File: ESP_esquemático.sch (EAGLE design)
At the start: 10 parts, among them U1 GY-521MPU6050

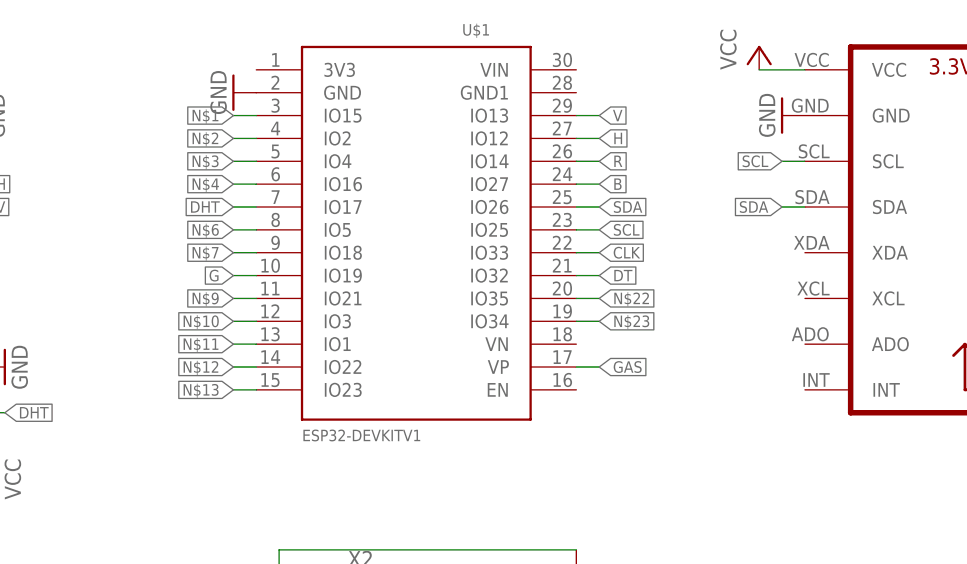
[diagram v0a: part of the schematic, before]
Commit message: adicionado código do arm
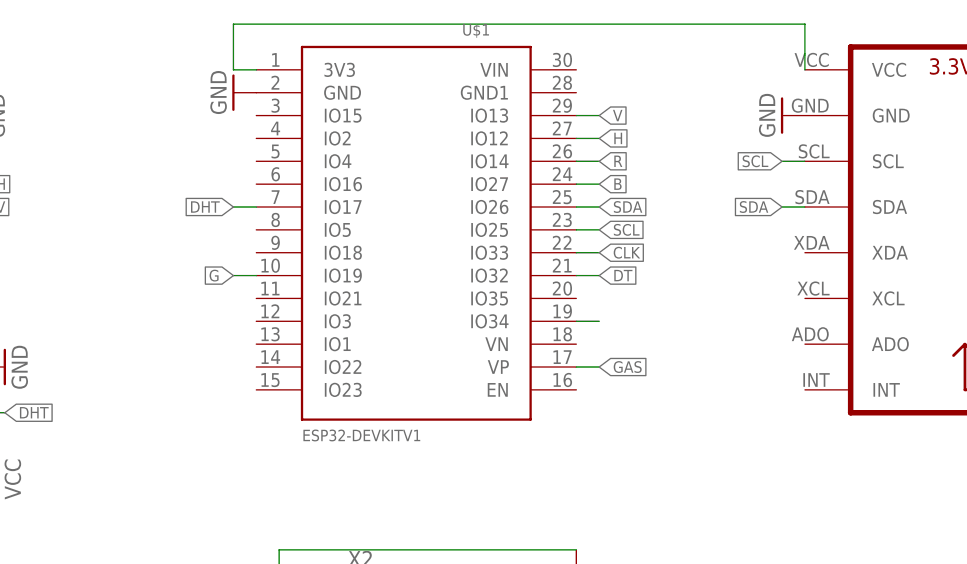
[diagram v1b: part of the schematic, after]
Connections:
- removed net N$10: U$1.IO3
- removed net N$11: U$1.IO1
- removed net N$12: U$1.IO22
- removed net N$13: U$1.IO23
- removed net N$2: U$1.IO2
- removed net N$22: U$1.IO35
- removed net N$3: U$1.IO4
- removed net N$4: U$1.IO16
- removed net N$6: U$1.IO5
- removed net N$7: U$1.IO18
- removed net N$9: U$1.IO21
- net N$1: now also U$1.3V3, U1.VCC; no longer U$1.IO15
- net VCC: no longer U1.VCC
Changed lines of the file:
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@@
 <part name="P+2" library="supply1" deviceset="VCC" device=""/>
 <part name="P+3" library="supply1" deviceset="VCC" device=""/>
-<part name="P+4" library="supply1" deviceset="VCC" device=""/>
 <part name="R1" library="rcl" deviceset="R-US_" device="0204/7" value="3k9"/>
 <part name="R2" library="rcl" deviceset="R-US_" device="0204/7" value="3k9"/>
@@
 <instance part="P+2" gate="VCC" x="33.02" y="10.16" rot="R90"/>
 <instance part="P+3" gate="VCC" x="2.54" y="30.48" rot="R180"/>
-<instance part="P+4" gate="VCC" x="88.9" y="78.74"/>
 <instance part="R1" gate="G$1" x="68.58" y="17.78" rot="R90"/>
 <instance part="R2" gate="G$1" x="71.12" y="0" rot="R90"/>
@@
 <wire x1="2.54" y1="33.02" x2="2.54" y2="35.56" width="0.1524" layer="91"/>
 </segment>
-<segment>
-<pinref part="U1" gate="G$1" pin="VCC"/>
-<pinref part="P+4" gate="VCC" pin="VCC"/>
-<wire x1="88.9" y1="76.2" x2="93.98" y2="76.2" width="0.1524" layer="91"/>
-</segment>
-</net>
-<net name="N$1" class="0">
-<segment>
-<pinref part="U$1" gate="G$1" pin="IO15"/>
-<wire x1="33.02" y1="71.12" x2="30.48" y2="71.12" width="0.1524" layer="91"/>
-<label x="30.48" y="71.12" size="1.27" layer="95" rot="R180" xref="yes"/>
-</segment>
-</net>
-<net name="N$2" class="0">
-<segment>
-<pinref part="U$1" gate="G$1" pin="IO2"/>
-<wire x1="33.02" y1="68.58" x2="30.48" y2="68.58" width="0.1524" layer="91"/>
-<label x="30.48" y="68.58" size="1.27" layer="95" rot="R180" xref="yes"/>
-</segment>
-</net>
-<net name="N$3" class="0">
-<segment>
-<pinref part="U$1" gate="G$1" pin="IO4"/>
-<wire x1="33.02" y1="66.04" x2="30.48" y2="66.04" width="0.1524" layer="91"/>
-<label x="30.48" y="66.04" size="1.27" layer="95" rot="R180" xref="yes"/>
-</segment>
-</net>
-<net name="N$4" class="0">
-<segment>
-<pinref part="U$1" gate="G$1" pin="IO16"/>
-<wire x1="33.02" y1="63.5" x2="30.48" y2="63.5" width="0.1524" layer="91"/>
-<label x="30.48" y="63.5" size="1.27" layer="95" rot="R180" xref="yes"/>
-</segment>
-</net>
-<net name="N$6" class="0">
-<segment>
-<pinref part="U$1" gate="G$1" pin="IO5"/>
-<wire x1="33.02" y1="58.42" x2="30.48" y2="58.42" width="0.1524" layer="91"/>
-<label x="30.48" y="58.42" size="1.27" layer="95" rot="R180" xref="yes"/>
-</segment>
-</net>
-<net name="N$7" class="0">
-<segment>
-<pinref part="U$1" gate="G$1" pin="IO18"/>
-<wire x1="33.02" y1="55.88" x2="30.48" y2="55.88" width="0.1524" layer="91"/>
-<label x="30.48" y="55.88" size="1.27" layer="95" rot="R180" xref="yes"/>
-</segment>
-</net>
-<net name="N$9" class="0">
-<segment>
-<pinref part="U$1" gate="G$1" pin="IO21"/>
-<wire x1="33.02" y1="50.8" x2="30.48" y2="50.8" width="0.1524" layer="91"/>
-<label x="30.48" y="50.8" size="1.27" layer="95" rot="R180" xref="yes"/>
-</segment>
-</net>
-<net name="N$10" class="0">
-<segment>
-<pinref part="U$1" gate="G$1" pin="IO3"/>
-<wire x1="33.02" y1="48.26" x2="30.48" y2="48.26" width="0.1524" layer="91"/>
-<label x="30.48" y="48.26" size="1.27" layer="95" rot="R180" xref="yes"/>
-</segment>
-</net>
-<net name="N$11" class="0">
-<segment>
-<pinref part="U$1" gate="G$1" pin="IO1"/>
-<wire x1="33.02" y1="45.72" x2="30.48" y2="45.72" width="0.1524" layer="91"/>
-<label x="30.48" y="45.72" size="1.27" layer="95" rot="R180" xref="yes"/>
-</segment>
-</net>
-<net name="N$12" class="0">
-<segment>
-<pinref part="U$1" gate="G$1" pin="IO22"/>
-<wire x1="33.02" y1="43.18" x2="30.48" y2="43.18" width="0.1524" layer="91"/>
-<label x="30.48" y="43.18" size="1.27" layer="95" rot="R180" xref="yes"/>
-</segment>
-</net>
-<net name="N$13" class="0">
-<segment>
-<pinref part="U$1" gate="G$1" pin="IO23"/>
-<wire x1="33.02" y1="40.64" x2="30.48" y2="40.64" width="0.1524" layer="91"/>
-<label x="30.48" y="40.64" size="1.27" layer="95" rot="R180" xref="yes"/>
-</segment>
-</net>
-<net name="N$22" class="0">
-<segment>
-<pinref part="U$1" gate="G$1" pin="IO35"/>
-<wire x1="68.58" y1="50.8" x2="71.12" y2="50.8" width="0.1524" layer="91"/>
-<label x="71.12" y="50.8" size="1.27" layer="95" xref="yes"/>
-</segment>
 </net>
 <net name="N$23" class="0">
@@
 <pinref part="U$1" gate="G$1" pin="IO34"/>
 <wire x1="68.58" y1="48.26" x2="71.12" y2="48.26" width="0.1524" layer="91"/>
-<label x="71.12" y="48.26" size="1.27" layer="95" xref="yes"/>
 </segment>
 </net>
@@
 </segment>
 </net>
+<net name="N$1" class="0">
+<segment>
+<pinref part="U$1" gate="G$1" pin="3V3"/>
+<wire x1="33.02" y1="76.2" x2="30.48" y2="76.2" width="0.1524" layer="91"/>
+<wire x1="30.48" y1="76.2" x2="30.48" y2="81.28" width="0.1524" layer="91"/>
+<pinref part="U1" gate="G$1" pin="VCC"/>
+<wire x1="30.48" y1="81.28" x2="93.98" y2="81.28" width="0.1524" layer="91"/>
+<wire x1="93.98" y1="81.28" x2="93.98" y2="76.2" width="0.1524" layer="91"/>
+</segment>
+</net>
